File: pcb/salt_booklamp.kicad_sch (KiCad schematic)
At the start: 28 parts, among them J1 USB-C31-S-RA-CS1E-BK-T/R, P1 PIC-TC2050-IDC, U1 PIC16F15213T-I/MF, U2 BQ21040DBVR, U3 TPS61158DRVR

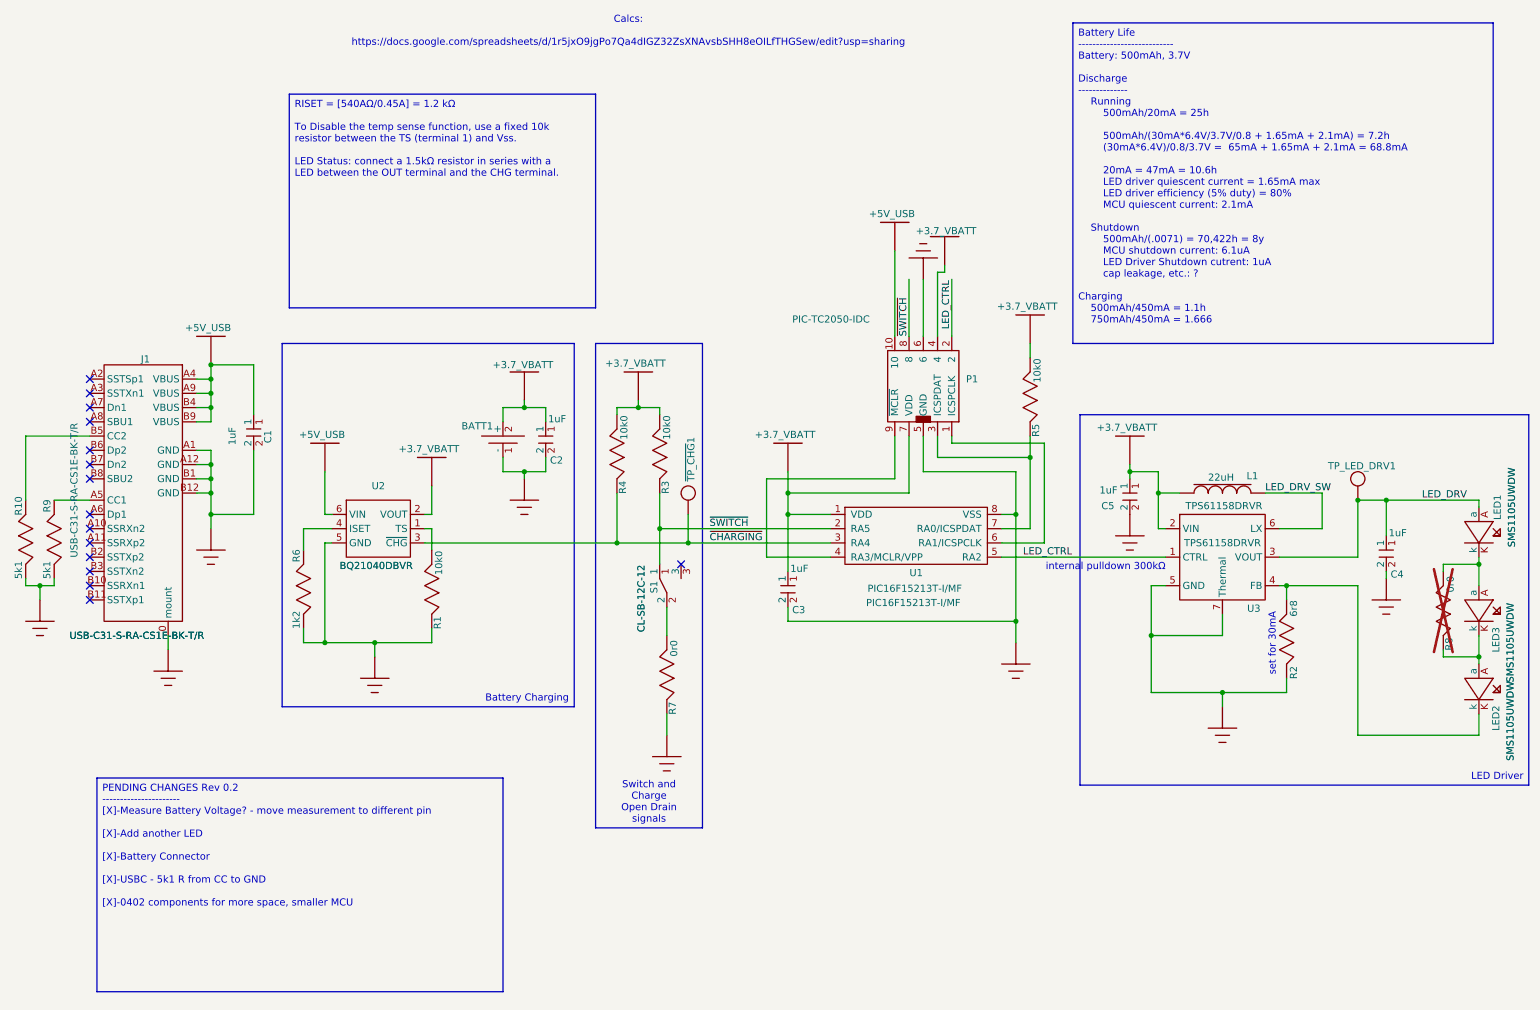
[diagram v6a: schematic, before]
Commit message: add test point and clean up schematic
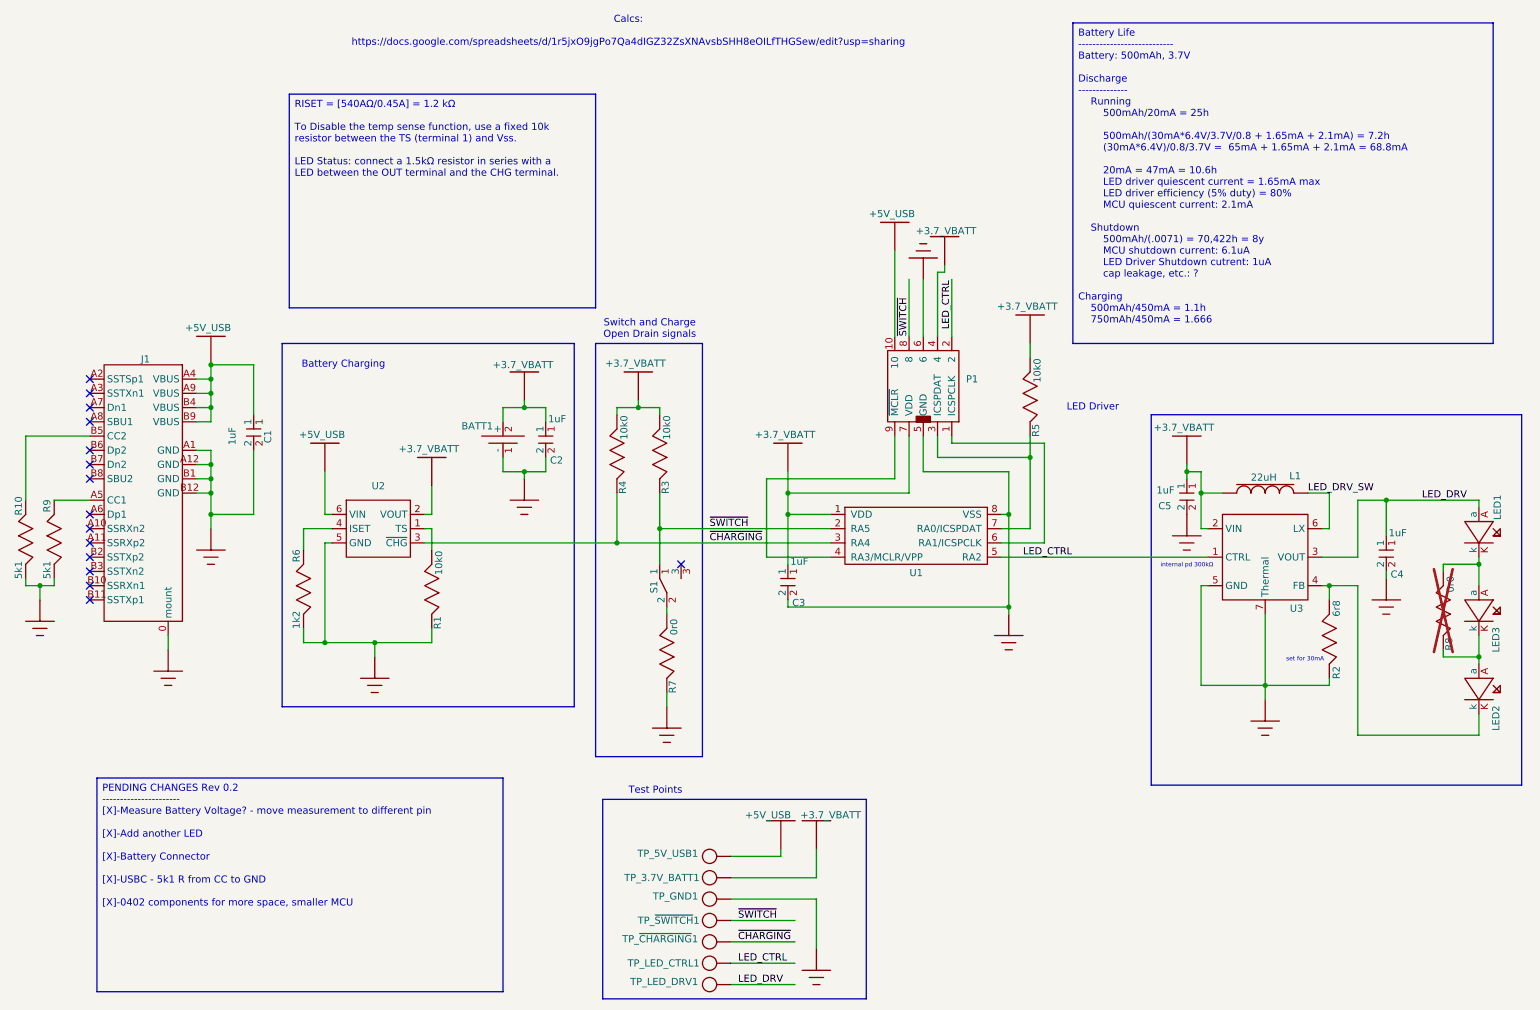
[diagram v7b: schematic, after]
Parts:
- added TP_GND1, TP_LED_CTRL1, TP_LED_DRV1, TP_~{CHARGING}1, TP_~{SWITCH}1: ~, salt_booklamp_footprints:1-pin header, symbol salt_booklamp:1-Pin_Header
- renumbered TP_LED_DRV1 to TP_3.7V_BATT1, ~{TP_CHG}1 to TP_5V_USB1
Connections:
- net +3.7_VBATT: now also TP_3.7V_BATT1.1
- net +5V_USB: now also TP_5V_USB1.1
- net GND: now also TP_GND1.1
- net LED_CTRL: now also TP_LED_CTRL1.1
- net LED_DRV: now also TP_LED_DRV1.1; no longer TP_3.7V_BATT1.1
- net ~{CHARGING}: now also TP_~{CHARGING}1.1; no longer TP_5V_USB1.1
- net ~{SWITCH}: now also TP_~{SWITCH}1.1
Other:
- note added: "Battery Charging"
- note added: "LED Driver"
- note added: "Switch and Charge Open Drain signals"
- note added: "Test Points"
- note added: "internal pd 300kΩ"
- note removed: "internal pulldown 300kΩ"
- moved on the sheet: C3, C5, L1, R2, R7, TP_3.7V_BATT1, TP_5V_USB1, U3

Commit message: Routing work
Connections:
- net +3.7_VBATT: no longer U2.2 (VOUT)
- net +5V_USB: now also U2.2 (VOUT); no longer U2.6 (VIN)
- net GND: now also U2.3 (~{CHG}); no longer U2.5 (GND)
- net ~{CHARGING}: no longer U2.3 (~{CHG})
- net at R1.2: no longer U2.1 (TS)
- net at R6.1: now also U2.1 (TS); no longer U2.4 (ISET)
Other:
- moved on the sheet: U2
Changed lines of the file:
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@@
 	)
 	(junction
+		(at 68.58 109.22)
+		(diameter 0)
+		(color 0 0 0 0)
+	)
+	(junction
 		(at 77.47 129.54)
 		(diameter 0)
@@
 	)
 	(junction
+		(at 68.58 111.76)
+		(diameter 0)
+		(color 0 0 0 0)
+	)
+	(junction
 		(at 124.46 87.63)
 		(diameter 0)
@@
 	)
 	(junction
+		(at 68.58 106.68)
+		(diameter 0)
+		(color 0 0 0 0)
+	)
+	(junction
 		(at 68.58 129.54)
 		(diameter 0)
@@
 	(wire
 		(pts
-			(xy 64.77 109.22) (xy 69.85 109.22)
+			(xy 64.77 109.22) (xy 68.58 109.22)
 		)
 		(stroke
@@
 	(wire
 		(pts
+			(xy 68.58 109.22) (xy 69.85 109.22)
+		)
+		(stroke
+			(width 0)
+			(type default)
+		)
+	)
+	(wire
+		(pts
 			(xy 48.26 100.33) (xy 48.26 102.87)
 		)
@@
 		(lib_id "salt_booklamp:batt_chg_ic_BQ21040DBVR")
 		(at 77.47 109.22 0)
+		(mirror y)
 		(unit 1)
 		(exclude_from_sim yes)
@@
 		(dnp no)
 		(property "Reference" "U2"
-			(at 78.105 101.6 0)
+			(at 76.835 101.6 0)
 			(effects
 				(font
@@
 		)
 		(property "Value" "BQ21040DBVR"
-			(at 77.724 115.824 0)
+			(at 77.216 115.824 0)
 			(effects
 				(font
@@
 		)
 		(property "Footprint" "salt_booklamp_footprints:BQ21040DBVR"
-			(at 77.978 117.094 0)
+			(at 76.962 117.094 0)
 			(effects
 				(font
@@
 		)
 		(property "Manufacturer Part Number" "BQ21040DBVR"
-			(at 77.724 115.824 0)
+			(at 77.216 115.824 0)
 			(effects
 				(font
